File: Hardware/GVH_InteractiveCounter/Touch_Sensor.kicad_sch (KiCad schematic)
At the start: 9 parts, among them J4 Electrode, U1 AT42QT1010

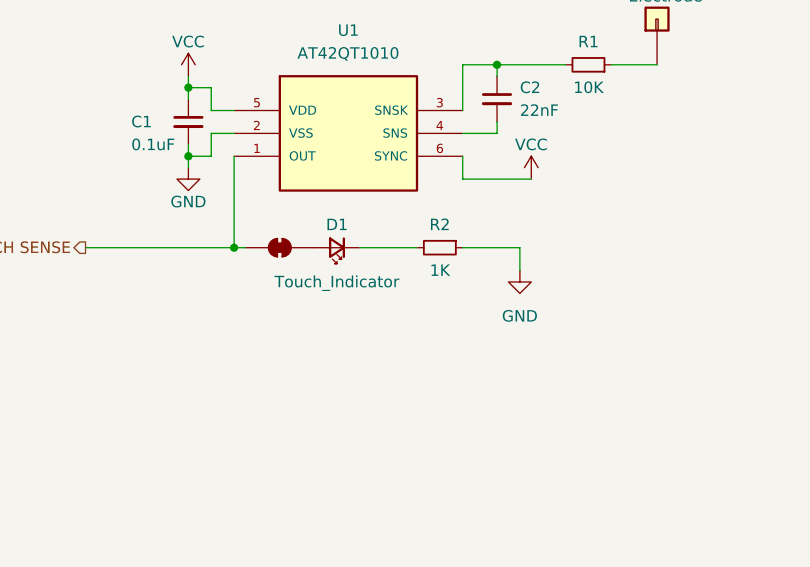
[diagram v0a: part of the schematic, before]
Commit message: Backing up work on PCB before some major changes
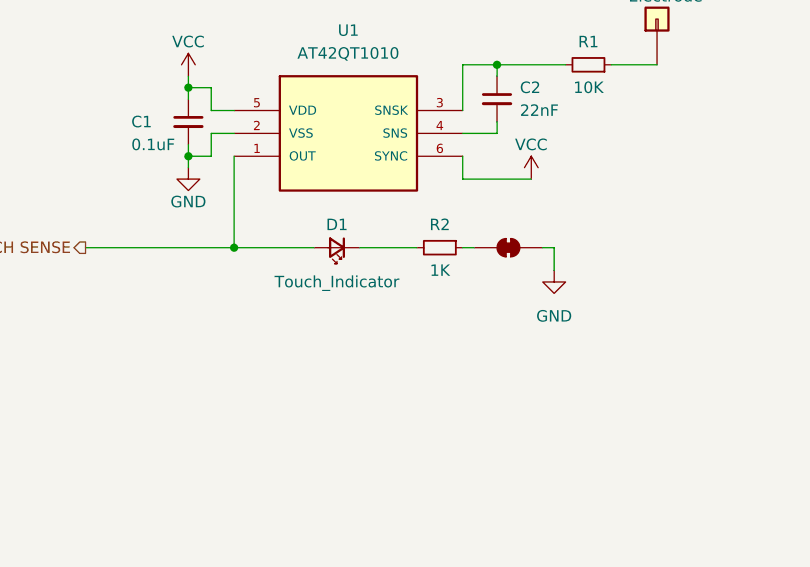
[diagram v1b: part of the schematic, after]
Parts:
- C1, C2: footprint Capacitor_SMD:C_1206_3216Metric_Pad1.33x1.80mm_HandSolder -> Capacitor_SMD:C_0805_2012Metric_Pad1.18x1.45mm_HandSolder
- D1: footprint LED_SMD:LED_1206_3216Metric_Pad1.42x1.75mm_HandSolder -> LED_SMD:LED_0805_2012Metric_Pad1.15x1.40mm_HandSolder
- R1, R2: footprint Resistor_SMD:R_1206_3216Metric_Pad1.30x1.75mm_HandSolder -> Resistor_SMD:R_0805_2012Metric_Pad1.20x1.40mm_HandSolder
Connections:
- net GND: now also JP1.2 (B); no longer R2.1
- net TOUCH SENSE: now also D1.2 (A); no longer JP1.1 (A)
- new net: JP1.1 (A), R2.1

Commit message: Board version 2 done. Not happy will start over
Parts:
- removed J4: Electrode, Connector_Pin:Pin_D1.3mm_L11.0mm_LooseFit, symbol Connector_Generic:Conn_01x01
- JP1: footprint Jumper:SolderJumper-2_P1.3mm_Bridged_RoundedPad1.0x1.5mm -> Jumper:SolderJumper-2_P1.3mm_Bridged_Pad1.0x1.5mm
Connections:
- net GND: now also R2.1; no longer JP1.2 (B)
- net TOUCH SENSE: now also JP1.1 (A); no longer D1.2 (A)
- net TOUCH_PAD: now reaches R1.1
- net VCC renamed +5V
- new net: D1.2 (A), JP1.2 (B)
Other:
- moved on the sheet: D1, R2

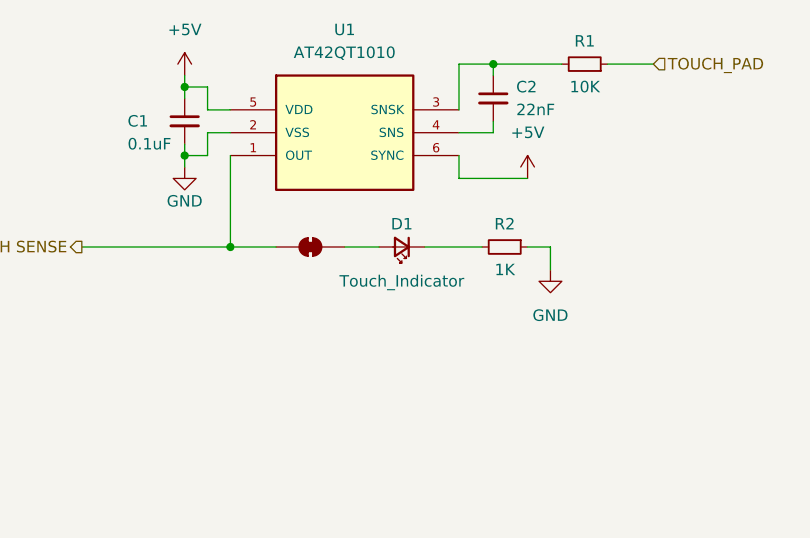
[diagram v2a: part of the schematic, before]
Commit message: Updated all of the parts to have the LCSC part numbers
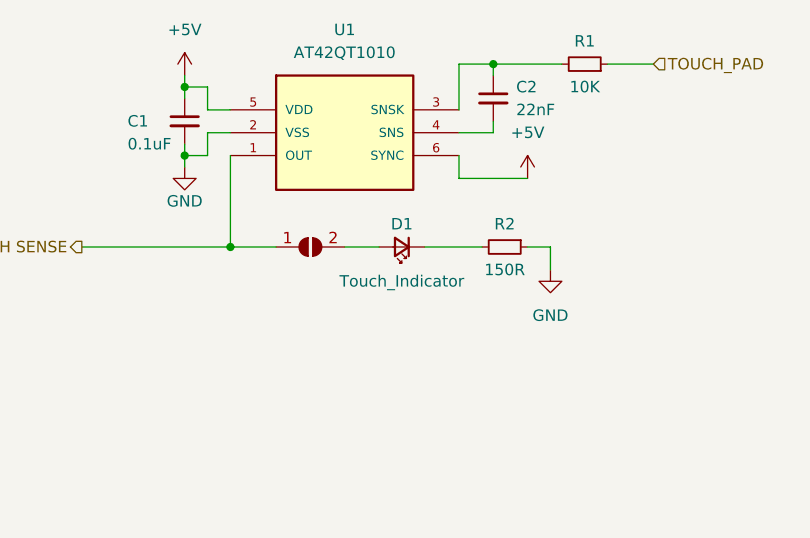
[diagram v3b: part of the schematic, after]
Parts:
- C1: LCSC (none) -> C15850
- C2: LCSC (none) -> C1729
- D1: LCSC (none) -> C2297
- JP1: footprint Jumper:SolderJumper-2_P1.3mm_Bridged_Pad1.0x1.5mm -> Jumper:SolderJumper-2_P1.3mm_Open_RoundedPad1.0x1.5mm; symbol Jumper:SolderJumper_2_Bridged -> Jumper:SolderJumper_2_Open; now left out of the parts list
- R1: LCSC (none) -> C17414
- R2: value 1K -> 150R; Digikey P/N 311-1.00KCRCT-ND -> 311-150CRCT-ND; Digikey Page https://www.digikey.com/en/products/detail/yageo/RC0805FR-071KL/727444 -> https://www.digikey.com/en/products/detail/yageo/RC0805FR-07150RL/727613; LCSC (none) -> C17471
- U1: LCSC (none) -> C74512; Package (none) -> SOT-23-6
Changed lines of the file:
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@@
+      (effects (font (size 1.27 1.27)) hide)
+    )
+    (property "LCSC" "C74512" (at 146.05 92.71 0)
+      (effects (font (size 1.27 1.27)) hide)
+    )
+    (property "Package" "SOT-23-6" (at 146.05 92.71 0)
       (effects (font (size 1.27 1.27)) hide)
     )
@@
     )
   )
-  (symbol (lib_id "Jumper:SolderJumper_2_Bridged") (at 142.24 105.41 0) (unit 1)
-    (in_bom yes) (on_board yes) (dnp no) (fields_autoplaced)
+  (symbol (lib_id "Jumper:SolderJumper_2_Open") (at 142.24 105.41 0) (unit 1)
+    (in_bom no) (on_board yes) (dnp no) (fields_autoplaced)
     (property "Reference" "JP1" (at 142.24 99.06 0)
       (effects (font (size 1.27 1.27)) hide)
@@
       (effects (font (size 1.27 1.27)) hide)
     )
-    (property "Footprint" "Jumper:SolderJumper-2_P1.3mm_Bridged_Pad1.0x1.5mm" (at 142.24 105.41 0)
+    (property "Footprint" "Jumper:SolderJumper-2_P1.3mm_Open_RoundedPad1.0x1.5mm" (at 142.24 105.41 0)
       (effects (font (size 1.27 1.27)) hide)
     )
@@
       (effects (font (size 1.27 1.27)) hide)
     )
+    (property "LCSC" "C1729" (at 162.56 88.9 0)
+      (effects (font (size 1.27 1.27)) hide)
+    )
     (pin "2")
     (pin "1")
@@
       (effects (font (size 1.27 1.27)) hide)
     )
+    (property "LCSC" "C15850" (at 128.27 91.44 0)
+      (effects (font (size 1.27 1.27)) hide)
+    )
     (pin "2")
     (pin "1")
@@
       (effects (font (size 1.27 1.27)) hide)
     )
+    (property "LCSC" "C17414" (at 172.72 85.09 90)
+      (effects (font (size 1.27 1.27)) hide)
+    )
     (pin "2")
     (pin "1")
@@
       (effects (font (size 1.27 1.27)))
     )
-    (property "Value" "1K" (at 163.83 107.95 90)
+    (property "Value" "150R" (at 163.83 107.95 90)
       (effects (font (size 1.27 1.27)))
     )
@@
       (effects (font (size 1.27 1.27)) hide)
     )
-    (property "Digikey P/N" "311-1.00KCRCT-ND" (at 163.83 105.41 90)
-      (effects (font (size 1.27 1.27)) hide)
-    )
-    (property "Digikey Page" "https://www.digikey.com/en/products/detail/yageo/RC0805FR-071KL/727444" (at 163.83 105.41 90)
+    (property "Digikey P/N" "311-150CRCT-ND" (at 163.83 105.41 90)
+      (effects (font (size 1.27 1.27)) hide)
+    )
+    (property "Digikey Page" "https://www.digikey.com/en/products/detail/yageo/RC0805FR-07150RL/727613" (at 163.83 105.41 90)
       (effects (font (size 1.27 1.27)) hide)
     )
     (property "Package" "0805" (at 163.83 105.41 0)
+      (effects (font (size 1.27 1.27)) hide)
+    )
+    (property "LCSC" "C17471" (at 163.83 105.41 90)
       (effects (font (size 1.27 1.27)) hide)
     )
@@
       (effects (font (size 1.27 1.27)) hide)
     )
+    (property "LCSC" "C2297" (at 152.4 105.41 0)
+      (effects (font (size 1.27 1.27)) hide)
+    )

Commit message: Layouts done and ordered.
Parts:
- C1: LCSC C15850 -> C1711
- C2: now left out of the parts list
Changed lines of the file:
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@@
   )
   (symbol (lib_id "Device:C_Small") (at 162.56 88.9 0) (unit 1)
-    (in_bom yes) (on_board yes) (dnp no)
+    (in_bom no) (on_board yes) (dnp no)
     (property "Reference" "C2" (at 165.1 87.6363 0)
       (effects (font (size 1.27 1.27)) (justify left))
@@
       (effects (font (size 1.27 1.27)) hide)
     )
-    (property "LCSC" "C15850" (at 128.27 91.44 0)
+    (property "LCSC" "C1711" (at 128.27 91.44 0)
       (effects (font (size 1.27 1.27)) hide)
     )
